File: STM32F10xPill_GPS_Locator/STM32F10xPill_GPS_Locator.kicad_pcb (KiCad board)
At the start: 2 copper layers, 70 x 91 mm, 114 parts, among them J1 Conn_01x03, J2 Conn_01x05, J3 Conn_01x02, J4 734120110, Q1 2301D, SW1 PTS645VH58-2 LFS, SW2 TS-1092S-B3D2-G, SW3 TS-1092S-B3D2-G, SW4 Power, SW5 TS-1092S-B3D2-G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

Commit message: Add USB Port
Added schematic for controlling SEL and PROG2 on the PPM, as well as USB filtering and ESD protection and stuff. The board layout was not changed yet
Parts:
- moved G*** 56.5 mm to (69.5, 111.0)
- moved REF** 14.2 mm to (127.5, 111.0)
- moved JP1 10.0 mm to (162.5, 98.5)
- moved D3 3.05 mm to (171.0, 111.0)
- moved D4 3.05 mm to (171.0, 109.0)
- moved R10 3.05 mm to (168.0, 111.0)
- moved R13 3.05 mm to (169.5, 112.5)
- moved R14 3.05 mm to (169.5, 107.5)
- moved R15 3.05 mm to (168.0, 109.0)
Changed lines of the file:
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@@
 	(footprint "Resistor_SMD:R_0402_1005Metric_Pad0.72x0.64mm_HandSolder"
 		(layer "F.Cu")
-		(at 172.2 111.0875)
+		(at 169.5 112.5)
 		(descr "Resistor SMD 0402 (1005 Metric), square (rectangular) end terminal, IPC_7351 nominal with elongated pad for handsoldering. (Body size source: IPC-SM-782 page 72, https://www.pcb-3d.com/wordpress/wp-content/uploads/ipc-sm-782a_amendment_1_and_2.pdf), generated with kicad-footprint-generator")
 		(tags "resistor handsolder")
@@
 	(footprint "Resistor_SMD:R_0402_1005Metric_Pad0.72x0.64mm_HandSolder"
 		(layer "F.Cu")
-		(at 170.7 109.5875)
+		(at 168 111)
 		(descr "Resistor SMD 0402 (1005 Metric), square (rectangular) end terminal, IPC_7351 nominal with elongated pad for handsoldering. (Body size source: IPC-SM-782 page 72, https://www.pcb-3d.com/wordpress/wp-content/uploads/ipc-sm-782a_amendment_1_and_2.pdf), generated with kicad-footprint-generator")
 		(tags "resistor handsolder")
@@
 		)
 		(model "/home/michaelp/Documents/Projects/STM32F1-GPS-Locator/Project Library/3D Models/Nokia5110.step"
+			(hide yes)
 			(offset
 				(xyz -41 13 11)
@@
 	(footprint "Resistor_SMD:R_0402_1005Metric_Pad0.72x0.64mm_HandSolder"
 		(layer "F.Cu")
-		(at 172.2 106.0875)
+		(at 169.5 107.5)
 		(descr "Resistor SMD 0402 (1005 Metric), square (rectangular) end terminal, IPC_7351 nominal with elongated pad for handsoldering. (Body size source: IPC-SM-782 page 72, https://www.pcb-3d.com/wordpress/wp-content/uploads/ipc-sm-782a_amendment_1_and_2.pdf), generated with kicad-footprint-generator")
 		(tags "resistor handsolder")
@@
 		(tags "capacitor")
 		(property "Reference" "C17"
-			(at 2.45 0 180)
+			(at -0.9625 -2.4125 180)
 			(layer "F.SilkS")
 			(effects
@@
 	(footprint "Resistor_SMD:R_0402_1005Metric_Pad0.72x0.64mm_HandSolder"
 		(layer "F.Cu")
-		(at 170.7 107.5875)
+		(at 168 109)
 		(descr "Resistor SMD 0402 (1005 Metric), square (rectangular) end terminal, IPC_7351 nominal with elongated pad for handsoldering. (Body size source: IPC-SM-782 page 72, https://www.pcb-3d.com/wordpress/wp-content/uploads/ipc-sm-782a_amendment_1_and_2.pdf), generated with kicad-footprint-generator")
 		(tags "resistor handsolder")
@@
 	(footprint "LED_SMD:LED_0603_1608Metric"
 		(layer "F.Cu")
-		(at 173.7 109.5875)
+		(at 171 111)
 		(descr "LED SMD 0603 (1608 Metric), square (rectangular) end terminal, IPC_7351 nominal, (Body size source: http://www.tortai-tech.com/upload/download/2011102023233369053.pdf), generated with kicad-footprint-generator")
 		(tags "LED")
@@
 	(footprint "Jumper:SolderJumper-2_P1.3mm_Open_Pad1.0x1.5mm"
 		(layer "F.Cu")
-		(at 172.4125 97.0875 90)
+		(at 162.5 98.5 90)
 		(descr "SMD Solder Jumper, 1x1.5mm Pads, 0.3mm gap, open")
 		(tags "solder jumper open")
 		(property "Reference" "JP1"
-			(at 0 -2.5 180)
+			(at -2.5 0 180)
 			(layer "F.SilkS")
 			(effects
@@
 		(tags "solder jumper open")
 		(property "Reference" "JP2"
-			(at -3 -2.5 0)
+			(at 3.4125 1.0875 0)
 			(layer "F.SilkS")
 			(effects
@@
 	(footprint "LED_SMD:LED_0603_1608Metric"
 		(layer "F.Cu")
-		(at 173.7 107.5875)
+		(at 171 109)
 		(descr "LED SMD 0603 (1608 Metric), square (rectangular) end terminal, IPC_7351 nominal, (Body size source: http://www.tortai-tech.com/upload/download/2011102023233369053.pdf), generated with kicad-footprint-generator")
 		(tags "LED")
@@
 	(footprint "Watermarks:michaelpate.net QR Code 10mm"
 		(layer "B.Cu")
-		(at 125.1125 125 180)
+		(at 127.5 111 180)
 		(property "Reference" "REF**"
 			(at 0 9 0)
@@
 	(footprint "LOGO"
 		(layer "B.Cu")
-		(at 126 109.5 90)
+		(at 69.5 111 90)
 		(property "Reference" "G***"
 			(at 0 0 90)
@@
 	)
 	(gr_text "BATT LOW"
-		(at 175.2 109.5875 0)
+		(at 172.5 111 0)
 		(layer "F.SilkS" knockout)
 		(effects
@@
 	)
 	(gr_text "MCU VDD"
-		(at 173.9125 97.0875 0)
+		(at 162.5 96 0)
 		(layer "F.SilkS" knockout)
 		(effects
@@
 				(bold yes)
 			)
-			(justify left)
 		)
 	)
@@
 	)
 	(gr_text "BATT CHARGE"
-		(at 175.2 107.5875 0)
+		(at 172.5 109 0)
 		(layer "F.SilkS" knockout)
 		(effects
@@
 	)
 	(gr_text "michaelpate.net"
-		(at 131.5 125 270)
+		(at 133.8875 111 270)
 		(layer "B.SilkS")
 		(effects
@@
 	)
 	(gr_text "geocaching.com"
-		(at 134 109.5 270)
+		(at 77.5 111 270)
 		(layer "B.SilkS")
 		(effects

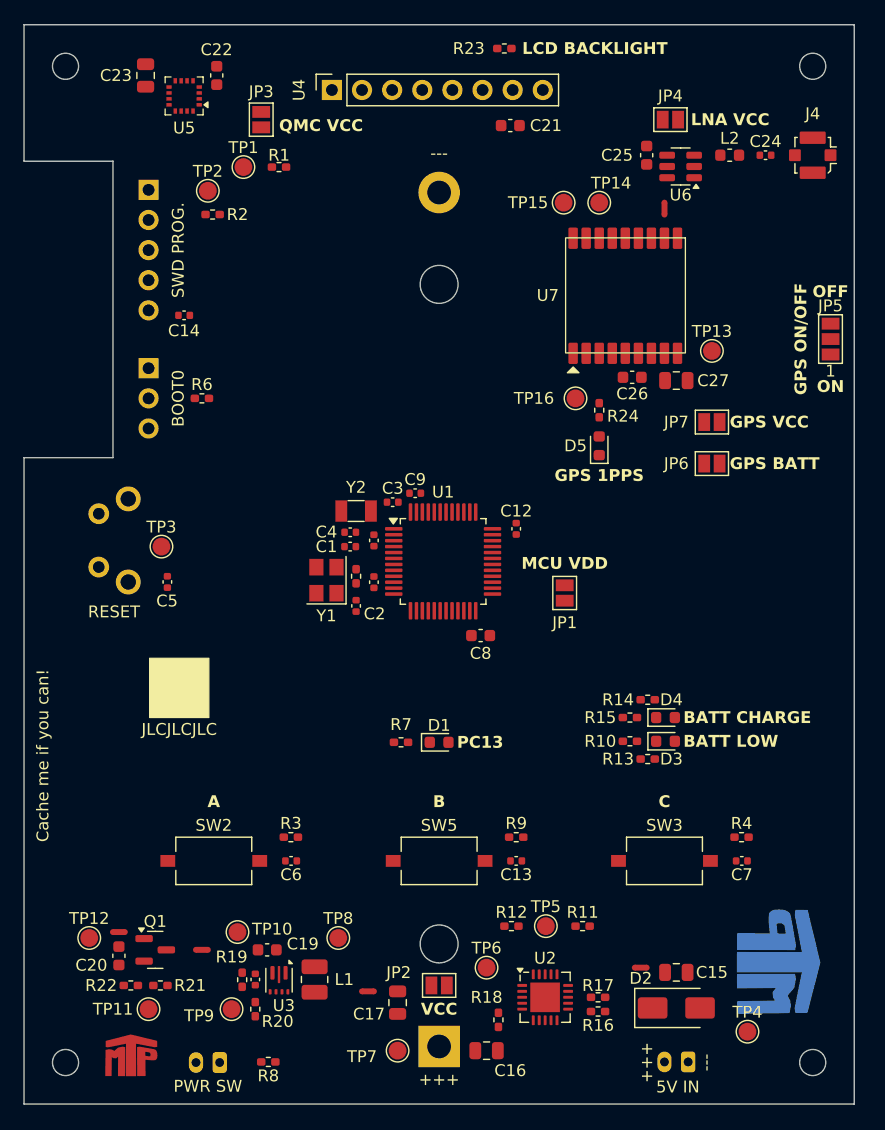
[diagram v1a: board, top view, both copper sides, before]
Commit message: Added SD card and updated PCB layout
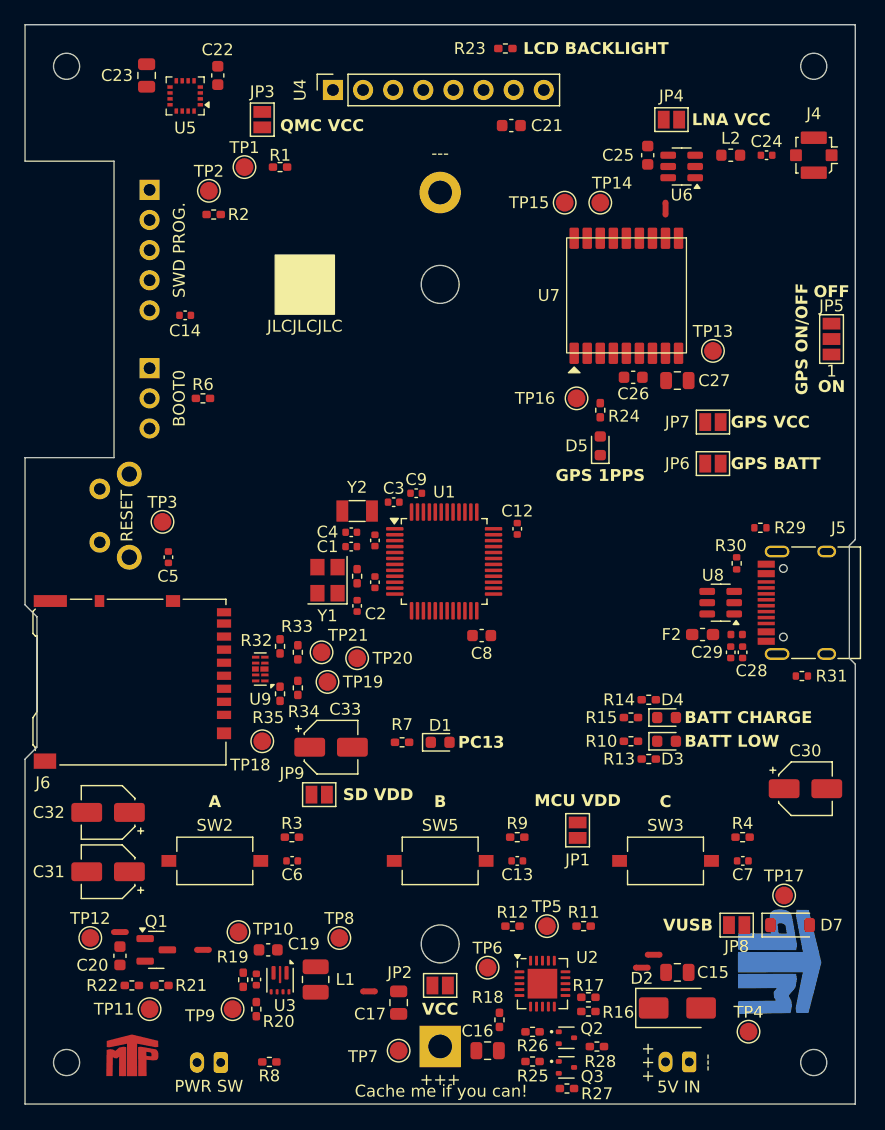
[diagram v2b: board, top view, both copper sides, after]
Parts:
- added C28: 10n, Capacitor_SMD:C_0402_1005Metric, F.Cu at (177.5, 103.5)
- added C29: 100n, Capacitor_SMD:C_0402_1005Metric, F.Cu at (176.5, 103.5)
- added C30: 4u7, Capacitor_SMD:CP_Elec_4x5.4, F.Cu at (182.8, 115.0)
- added C31: 10u, Capacitor_SMD:CP_Elec_4x5.4, F.Cu at (124.0, 122.0)
- added C32: 10u, Capacitor_SMD:CP_Elec_4x5.4, F.Cu at (124.0, 117.0)
- added C33: 47u, Capacitor_SMD:CP_Elec_4x5.4, F.Cu at (142.8, 111.5)
- added D7: MBR0520T1G-JSM, Diode_SMD:D_SOD-123, F.Cu at (181.5, 126.5)
- added F2: 0603L020/6XR, Fuse:Fuse_0603_1608Metric_Pad1.05x0.95mm_HandSolder, F.Cu at (174.1, 102.0)
- added FB2: 33R100MHz, Inductor_SMD:L_0402_1005Metric, F.Cu at (177.0, 102.0)
- added J5: TYPE-C-31-M-12, Connector_USB:USB_C_Receptacle_HRO_TYPE-C-31-M-12, F.Cu at (183.5, 99.3)
- added J6: Micro_SD_Card, Connector_Card:microSD_HC_Hirose_DM3AT-SF-PEJM5, F.Cu at (126.1, 106.0)
- added JP8: Jumper_2_Open, Jumper:SolderJumper-2_P1.3mm_Open_Pad1.0x1.5mm, F.Cu at (177.0, 126.5)
- added JP9: Jumper_2_Open, Jumper:SolderJumper-2_P1.3mm_Open_Pad1.0x1.5mm, F.Cu at (141.8, 115.5)
- added NT6: NetTie_2, NetTie:NetTie-2_SMD_Pad0.5mm, F.Cu at (170.0, 129.0)
- added Q2: 2SK3019-ES, Package_TO_SOT_SMD:SOT-523, F.Cu at (162.6, 136.0)
- added Q3: 2SK3019-ES, Package_TO_SOT_SMD:SOT-523, F.Cu at (162.6, 138.5)
- added R25: 10k, Resistor_SMD:R_0402_1005Metric_Pad0.72x0.64mm_HandSolder, F.Cu at (159.8, 138.0)
- added R26: 10k, Resistor_SMD:R_0402_1005Metric_Pad0.72x0.64mm_HandSolder, F.Cu at (159.8, 135.5)
- added R27: 10k, Resistor_SMD:R_0402_1005Metric_Pad0.72x0.64mm_HandSolder, F.Cu at (162.7, 140.3)
- added R28: 10k, Resistor_SMD:R_0402_1005Metric_Pad0.72x0.64mm_HandSolder, F.Cu at (165.2, 136.7)
- added R29: 0, Resistor_SMD:R_0402_1005Metric, F.Cu at (179.0, 93.0)
- added R30: 5k1, Resistor_SMD:R_0402_1005Metric, F.Cu at (177.0, 96.0)
- added R31: 5k1, Resistor_SMD:R_0402_1005Metric, F.Cu at (182.5, 105.5)
- added R32: 4k7, Resistor_SMD:R_0402_1005Metric_Pad0.72x0.64mm_HandSolder, F.Cu at (138.5, 103.0)
- added R33: 4k7, Resistor_SMD:R_0402_1005Metric_Pad0.72x0.64mm_HandSolder, F.Cu at (140.0, 103.5)
- added R34: 4k7, Resistor_SMD:R_0402_1005Metric_Pad0.72x0.64mm_HandSolder, F.Cu at (140.0, 106.5)
- added R35: 4k7, Resistor_SMD:R_0402_1005Metric_Pad0.72x0.64mm_HandSolder, F.Cu at (138.5, 107.0)
- added TP17: USB_REC, TestPoint:TestPoint_Pad_D1.5mm, F.Cu at (181.0, 124.0)
- added TP18: SD_CS, TestPoint:TestPoint_Pad_D1.5mm, F.Cu at (137.0, 111.0)
- added TP19: SD_MOSI, TestPoint:TestPoint_Pad_D1.5mm, F.Cu at (142.5, 106.0)
- added TP20: SD_CLK, TestPoint:TestPoint_Pad_D1.5mm, F.Cu at (145.0, 104.0)
- added TP21: SD_MISO, TestPoint:TestPoint_Pad_D1.5mm, F.Cu at (142.0, 103.5)
- added U8: USBLC6-2SC6, Package_TO_SOT_SMD:SOT-23-6, F.Cu at (175.7, 99.3)
- added U9: TPD4E05U06DQAR, Package_DFN_QFN:Diodes_UDFN-10_1.0x2.5mm_P0.5mm, F.Cu at (136.8, 104.9)
- TP4: value PPM_IN -> 5V_IN
- moved JP1 20.0 mm to (163.6, 118.5)
- moved TP3 2.09 mm to (128.6, 92.5)
- moved SW1 2.09 mm to (123.3, 89.7)
- moved C5 2.09 mm to (129.1, 95.5)
- moved U2 1.17 mm to (160.6, 131.4)
- moved R16 0.81 mm to (164.5, 133.8)
- moved R17 0.81 mm to (164.5, 132.6)
- moved BT1 0.09 mm to (152.0, 136.7)
- moved C1 0.09 mm to (144.5, 94.6)
- moved C10 0.09 mm to (146.5, 94.1)
- moved C11 0.09 mm to (146.5, 97.6)
- moved C12 0.09 mm to (158.5, 93.1)
- moved C13 0.09 mm to (158.5, 121.1)
- moved C14 0.09 mm to (130.5, 75.1)
- moved C15 0.09 mm to (172.0, 130.5)
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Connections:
- R12 pad 1: GND -> /Power Supply/PPM_VPCC
- R12 pad 2: /Power Supply/PPM_VPCC -> GND
- U1 pad 32: unconnected-(U1-PA11-Pad32) -> USB_DM
- U1 pad 33: unconnected-(U1-PA12-Pad33) -> USB_DP
- U2 pad 3: +3.3V -> Net-(Q2-D)
- U2 pad 4: +3.3V -> Net-(Q3-D)
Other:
- outline, holes or cut-outs redrawn
- board text added: "SD VDD"
- board text added: "VUSB"

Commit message: Small changes to pcb
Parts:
- moved C22 1.00 mm to (132.2, 54.9)
- moved C23 1.00 mm to (126.2, 54.9)
- moved U5 1.00 mm to (129.5, 56.6)
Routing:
- added copper zone on B.Cu, net GND
- added copper zone on F.Cu, net GND
- added copper zone on In1.Cu, net GND
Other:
- copper layers 2 -> 4
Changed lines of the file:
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@@
 	(layers
 		(0 "F.Cu" signal)
+		(4 "In1.Cu" signal)
+		(6 "In2.Cu" signal)
 		(2 "B.Cu" signal)
 		(9 "F.Adhes" user "F.Adhesive")
@@
 	)
 	(setup
+		(stackup
+			(layer "F.SilkS"
+				(type "Top Silk Screen")
+			)
+			(layer "F.Paste"
+				(type "Top Solder Paste")
+			)
+			(layer "F.Mask"
+				(type "Top Solder Mask")
+				(thickness 0.01)
+			)
+			(layer "F.Cu"
+				(type "copper")
+				(thickness 0.035)
+			)
+			(layer "dielectric 1"
+				(type "prepreg")
+				(thickness 0.1)
+				(material "FR4")
+				(epsilon_r 4.5)
+				(loss_tangent 0.02)
+			)
+			(layer "In1.Cu"
+				(type "copper")
+				(thickness 0.035)
+			)
+			(layer "dielectric 2"
+				(type "core")
+				(thickness 1.24)
+				(material "FR4")
+				(epsilon_r 4.5)
+				(loss_tangent 0.02)
+			)
+			(layer "In2.Cu"
+				(type "copper")
+				(thickness 0.035)
+			)
+			(layer "dielectric 3"
+				(type "prepreg")
+				(thickness 0.1)
+				(material "FR4")
+				(epsilon_r 4.5)
+				(loss_tangent 0.02)
+			)
+			(layer "B.Cu"
+				(type "copper")
+				(thickness 0.035)
+			)
+			(layer "B.Mask"
+				(type "Bottom Solder Mask")
+				(thickness 0.01)
+			)
+			(layer "B.Paste"
+				(type "Bottom Solder Paste")
+			)
+			(layer "B.SilkS"
+				(type "Bottom Silk Screen")
+			)
+			(copper_finish "None")
+			(dielectric_constraints no)
+		)
 		(pad_to_mask_clearance 0)
 		(allow_soldermask_bridges_in_footprints no)
@@
 	(footprint "Package_LGA:LGA-16_3x3mm_P0.5mm"
 		(layer "F.Cu")
-		(at 130.5 56.5875 180)
+		(at 129.5 56.5875 180)
 		(descr "http://www.memsic.com/userfiles/files/DataSheets/Magnetic-Sensors-Datasheets/MMC5883MA-RevC.pdf")
 		(tags "lga land grid array")
@@
 			(polygon
 				(pts
-					(xy 131.5 57.5875) (xy 131.5 55.5875) (xy 129.5 55.5875) (xy 129.5 57.5875)
+					(xy 130.5 57.5875) (xy 130.5 55.5875) (xy 128.5 55.5875) (xy 128.5 57.5875)
 				)
 			)
@@
 	(footprint "Capacitor_SMD:C_0805_2012Metric"
 		(layer "F.Cu")
-		(at 127.25 54.8625 -90)
+		(at 126.25 54.8625 -90)
 		(descr "Capacitor SMD 0805 (2012 Metric), square (rectangular) end terminal, IPC_7351 nominal, (Body size source: IPC-SM-782 page 76, https://www.pcb-3d.com/wordpress/wp-content/uploads/ipc-sm-782a_amendment_1_and_2.pdf, https://docs.google.com/spreadsheets/d/1BsfQQcO9C6DZCsRaXUlFlo91Tg2WpOkGARC1WS5S8t0/edit?usp=sharing), generated with kicad-footprint-generator")
 		(tags "capacitor")
@@
 	(footprint "Capacitor_SMD:C_0603_1608Metric"
 		(layer "F.Cu")
-		(at 133.25 54.8625 -90)
+		(at 132.25 54.8625 -90)
 		(descr "Capacitor SMD 0603 (1608 Metric), square (rectangular) end terminal, IPC_7351 nominal, (Body size source: IPC-SM-782 page 76, https://www.pcb-3d.com/wordpress/wp-content/uploads/ipc-sm-782a_amendment_1_and_2.pdf), generated with kicad-footprint-generator")
 		(tags "capacitor")
@@
 			)
 		)
+	)
+	(zone
+		(net 10)
+		(net_name "GND")
+		(layer "F.Cu")
+		(hatch edge 0.5)
+		(priority 2)
+		(connect_pads
+			(clearance 0)
+		)
+		(min_thickness 0.25)
+		(filled_areas_thickness no)
+		(fill yes
+			(thermal_gap 0.5)
+			(thermal_bridge_width 0.9)
+		)
+		(polygon
+			(pts
+				(xy 187 50.5) (xy 117 50.5) (xy 117 141.5) (xy 187 141.5)
+			)
+		)
+	)
+	(zone
+		(net 0)
+		(net_name "")
+		(layers "F.Cu" "B.Cu" "In1.Cu" "In2.Cu")
+		(hatch edge 0.5)
+		(connect_pads
+			(clearance 0)
+		)
+		(min_thickness 0.25)
+		(filled_areas_thickness no)
+		(keepout
+			(tracks allowed)
+			(vias allowed)
+			(pads allowed)
+			(copperpour not_allowed)
+			(footprints allowed)
+		)
+		(placement
+			(enabled no)
+			(sheetname "")
+		)
+		(fill
+			(thermal_gap 0.5)
+			(thermal_bridge_width 0.9)
+		)
+		(polygon
+			(pts
+				(xy 187 56.5) (xy 160.5 56.5) (xy 160.5 78.5) (xy 187 78.5)
+			)
+		)
+	)
+	(zone
+		(net 0)
+		(net_name "")
+		(layers "F.Cu" "B.Cu" "In1.Cu" "In2.Cu")
+		(hatch edge 0.5)
+		(connect_pads
+			(clearance 0)
+		)
+		(min_thickness 0.25)
+		(filled_areas_thickness no)
+		(keepout
+			(tracks allowed)
+			(vias allowed)
+			(pads allowed)
+			(copperpour not_allowed)
+			(footprints allowed)
+		)
+		(placement
+			(enabled no)
+			(sheetname "")
+		)
+		(fill
+			(thermal_gap 0.5)
+			(thermal_bridge_width 0.9)
+		)
+		(polygon
+			(pts
+				(xy 135.5 50.5) (xy 117 50.5) (xy 117 62) (xy 135.5 62)
+			)
+		)
+	)
+	(zone
+		(net 10)
+		(net_name "GND")
+		(layer "B.Cu")
+		(hatch edge 0.5)
+		(priority 1)
+		(connect_pads
+			(clearance 0)
+		)
+		(min_thickness 0.25)
+		(filled_areas_thickness no)
+		(fill yes
+			(thermal_gap 0.5)
+			(thermal_bridge_width 0.9)
+		)
+		(polygon
+			(pts
+				(xy 187 50.5) (xy 117 50.5) (xy 117 141.5) (xy 187 141.5)
+			)
+		)
+	)
+	(zone
+		(net 10)
+		(net_name "GND")
+		(layer "In1.Cu")
+		(hatch edge 0.5)
+		(connect_pads
+			(clearance 0.5)
+		)
+		(min_thickness 0.25)
+		(filled_areas_thickness no)
+		(fill yes
+			(thermal_gap 0.5)
+			(thermal_bridge_width 0.9)
+		)
+		(polygon
+			(pts
+				(xy 117 50.5) (xy 117 141.5) (xy 187 141.5) (xy 187 50.5)
+			)
+		)
